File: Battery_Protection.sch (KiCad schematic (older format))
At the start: 0 parts

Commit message: Battery protection sch done. Assigned 99% of footprints. Layout is gonna be rough.
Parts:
- added C1, C10, C11, C2, C3, C4, C6, C7, C8, C9: C, Capacitor_SMD:C_0201_0603Metric, symbol Device:C
- added C12: 2.2u, Capacitor_SMD:C_0201_0603Metric, symbol Device:C
- added C13, C16: 0.1u 50v, Capacitor_SMD:C_0201_0603Metric, symbol Device:C
- added C14, C5: 0.1uF, Capacitor_SMD:C_0201_0603Metric, symbol Device:C
- added C15: 0.1u, Capacitor_SMD:C_0201_0603Metric, symbol Device:C
- added D1, D2, D3, D5, D6: LED, Diode_THT:D_DO-15_P3.81mm_Vertical_AnodeUp, symbol Device:LED
- added D4: DIODE, Diode_SMD:D_0201_0603Metric, symbol pspice:DIODE
- added F1, F2, F3, F4, F5, F6, F7, F8: Fuse_Small, Fuse:Fuse_1206_3216Metric_Pad1.42x1.75mm_HandSolder, symbol Device:Fuse_Small
- added J10, J11, J4, J5, J6, J7, J8, J9: Conn_01x02, Connector_JST:JST_PH_S2B-PH-K_1x02_P2.00mm_Horizontal, symbol Connector_Generic:Conn_01x02
- added Q1, Q6: 2n7002K, Package_TO_SOT_SMD:SOT-23, symbol Device:Q_NMOS_GSD
- added Q2, Q3, Q4, Q5: AO4468, Package_TO_SOT_SMD:TDSON-8-1, symbol Device:Q_NMOS_GSD
- added R1, R10, R2, R3, R4: 1k, Resistor_SMD:R_0201_0603Metric, symbol Device:R_US
- added R11, R12, R13, R19, R23, R24, R9: 100, Resistor_SMD:R_0201_0603Metric, symbol Device:R_US
- added R14: 51k, Resistor_SMD:R_0201_0603Metric, symbol Device:R_US
- added R15, R20, R22, R25, R29, R30: 5.1k, Resistor_SMD:R_0201_0603Metric, symbol Device:R_US
- added R16: 10Meg, Resistor_SMD:R_0201_0603Metric, symbol Device:R_US
- added R17: DNP, Resistor_SMD:R_0201_0603Metric, symbol Device:R_US
- added R18: 0, Resistor_SMD:R_0201_0603Metric, symbol Device:R_US
- added R21: 0.001, Resistor_SMD:R_1206_3216Metric, symbol Device:R_US
- added R26, R28: 10k, Resistor_SMD:R_0201_0603Metric, symbol Device:R_US
- added R27: 10M, Resistor_SMD:R_0201_0603Metric, symbol Device:R_US
- added R5, R6, R7, R8: 1 mOhm, Resistor_SMD:R_1206_3216Metric, symbol Device:R_US
- added SW1, SW2: SW_Push, Button_Switch_SMD:SW_Push_1P1T_NO_6x6mm_H9.5mm, symbol Switch:SW_Push
- added TH1: NCP18WF104F03, Resistor_SMD:R_0805_2012Metric, symbol Device:Thermistor_PTC
- added TH2, TH3, TH4, TH5: NXRT15WB473FA1B030, Diode_THT:D_A-405_P2.54mm_Vertical_AnodeUp, symbol Device:Thermistor_PTC_US
- added TP10, TP11, TP12, TP13, TP14, TP15, TP16, TP17, TP18, TP19, TP20, TP21, TP22, TP23, TP24, TP9: TestPoint, TestPoint:TestPoint_Pad_D2.0mm, symbol Connector:TestPoint
- added U101: BQ2947xx, Package_SON:WSON-8-1EP_2x2mm_P0.5mm_EP0.9x1.6mm, symbol SmartBattery:BQ2947xx
- added U102: BQ40Z50, Package_DFN_QFN:QFN-32-1EP_4x4mm_P0.4mm_EP2.65x2.65mm, symbol SmartBattery:BQ40Z50
- added U103: ITV4030, symbol SmartBattery:ITV4030
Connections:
- net labels added: BATT_SHUTDOWN, BAT_VN_0, BAT_VN_1, BAT_VN_2, BAT_VN_3, BAT_VP_0, BAT_VP_1, BAT_VP_2, BAT_VP_3, BTP_INT, FUSE_HEATER, GND, GNDA, PACK_+, SMB_C, SMB_D
- wire segments 0 -> 303
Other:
- note added: "LED = 333-2SURC/S530-A3\n5 mm DIP\n"

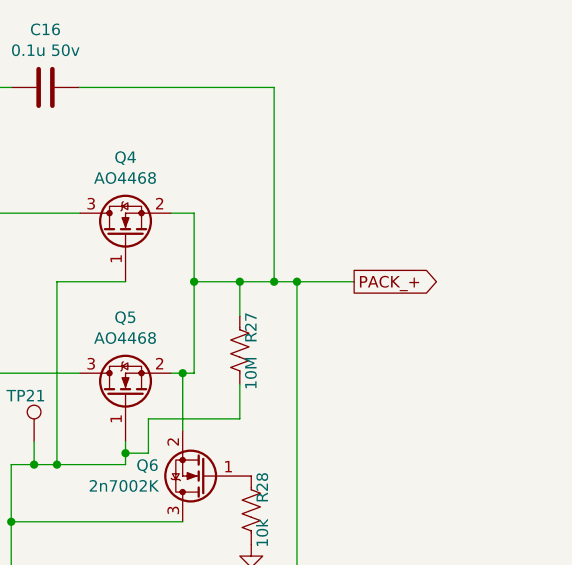
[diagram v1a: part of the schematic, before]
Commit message: Finished battery protection, starting charger page
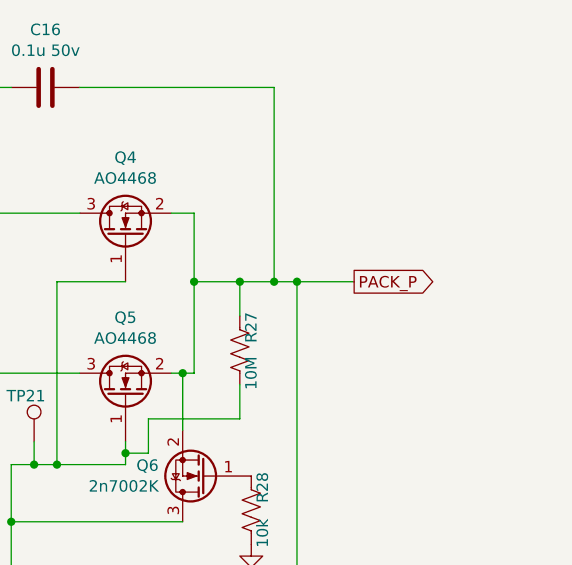
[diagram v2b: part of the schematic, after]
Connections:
- net labels added: PACK_P
- net labels removed: PACK_+
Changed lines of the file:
@@
 $Descr A4 11693 8268
 encoding utf-8
-Sheet 2 2
+Sheet 2 3
 Title ""
 Date ""
@@
 	8900 1650 8900 1350
 Text GLabel 9600 1650 2    50   Output ~ 0
-PACK_+
+PACK_P
 Connection ~ 9350 1650
 Wire Wire Line

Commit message: Added capacitors, inductors to charger page. Fixed capacitor sizes.
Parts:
- removed R7: 1 mOhm, Resistor_SMD:R_1206_3216Metric, symbol Device:R_US
- added TP18: TestPoint, TestPoint:TestPoint_Pad_D2.0mm, symbol Connector:TestPoint
- C18: renamed from C1; value C -> 0.1u 6.3v
- C19: renamed from C2; value C -> 0.1u 6.3v
- C20: renamed from C3; value C -> 0.1u 6.3v
- C21: renamed from C4; value C -> 0.1u 6.3v
- C22: renamed from C5; value 0.1uF -> 0.1uF 25v; footprint Capacitor_SMD:C_0201_0603Metric -> Capacitor_SMD:C_0402_1005Metric
- C23: renamed from C6; value C -> 0.1u 6.3v
- C24: renamed from C7; value C -> 0.1u 6.3v
- C25: renamed from C8; value C -> 0.1u 6.3v
- C26: renamed from C9; value C -> 0.1u 6.3v
- C27: renamed from C10; value C -> 0.1u 20v; footprint Capacitor_SMD:C_0201_0603Metric -> Capacitor_SMD:C_0402_1005Metric
- C28: renamed from C11; value C -> 0.1u 20v; footprint Capacitor_SMD:C_0201_0603Metric -> Capacitor_SMD:C_0402_1005Metric
- C29: renamed from C12; value 2.2u -> 2.2u 50v; footprint Capacitor_SMD:C_0201_0603Metric -> Capacitor_SMD:C_0603_1608Metric
- C30: renamed from C13; footprint Capacitor_SMD:C_0201_0603Metric -> Capacitor_SMD:C_0603_1608Metric
- C32: renamed from C15; value 0.1u -> 0.1u 6.3v
- C33: renamed from C16; footprint Capacitor_SMD:C_0201_0603Metric -> Capacitor_SMD:C_0603_1608Metric
- U2: renamed from U101; value BQ2947xx -> BQ294706DSGR
- renumbered C14 to C31, D1 to D2, D2 to D3, D3 to D4, D4 to D5, D5 to D6, D6 to D7, Q1 to Q2, Q2 to Q3, Q3 to Q4, Q4 to Q5, Q5 to Q6, Q6 to Q7, R8 to R10, R9 to R11, R10 to R12, R11 to R13, R12 to R14, R13 to R15, R14 to R16, R15 to R17, R16 to R18, R17 to R19, R18 to R20, R19 to R21, R20 to R22, R21 to R23, R22 to R24, R23 to R25, R24 to R26, R25 to R27, R26 to R28, R27 to R29, R1 to R3, R28 to R30, R29 to R31, R30 to R32, R2 to R4, R3 to R5, R4 to R6, R5 to R7, R6 to R8, TP17 to TP10, TP18 to TP11, TP19 to TP12, TP20 to TP13, TP21 to TP14, TP22 to TP15, TP23 to TP16, TP24 to TP17, TP9 to TP2, TP10 to TP3, TP11 to TP4, TP12 to TP5, TP13 to TP6, TP14 to TP7, TP15 to TP8, TP16 to TP9, U103 to U3, U102 to U4
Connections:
- net labels added: BATT_INT, BATT_PACK_P, BATT_SHUTDOWN_N, BATT_SMB_C, BATT_SMB_D
- net labels removed: BATT_SHUTDOWN, BTP_INT, PACK_P, SMB_C, SMB_D

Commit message: Added bunch of cap to charger, made footprint for diode + fuse
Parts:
- U3: footprint (none) -> SmartBattery:ITV4030
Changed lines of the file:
@@
 F 0 "U3" H 5600 2075 50  0000 C CNN
 F 1 "ITV4030" H 5600 1984 50  0000 C CNN
-F 2 "" H 5600 1700 50  0001 C CNN
+F 2 "SmartBattery:ITV4030" H 5600 1700 50  0001 C CNN
 F 3 "" H 5600 1700 50  0001 C CNN
 	1    5600 1700

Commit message: Adding lots of changes. Started output Stage
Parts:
- removed J10, J11, J4, J5, J6, J7, J8, J9: Conn_01x02, Connector_JST:JST_PH_S2B-PH-K_1x02_P2.00mm_Horizontal, symbol Connector_Generic:Conn_01x02
- removed Q3, Q4, Q5, Q6: AO4468, Package_TO_SOT_SMD:TDSON-8-1, symbol Device:Q_NMOS_GSD
- added J10, J11, J4, J5, J6, J7, J8, J9: JST 2P-1.0, Connector_JST:JST_SH_SM02B-SRSS-TB_1x02-1MP_P1.00mm_Horizontal, symbol Connector_Generic_MountingPin:Conn_01x02_MountingPin
- added Q4, Q6: AO4468, SmartBattery:SOIC-8_Alpha_Omega, symbol SmartBattery:AO4468

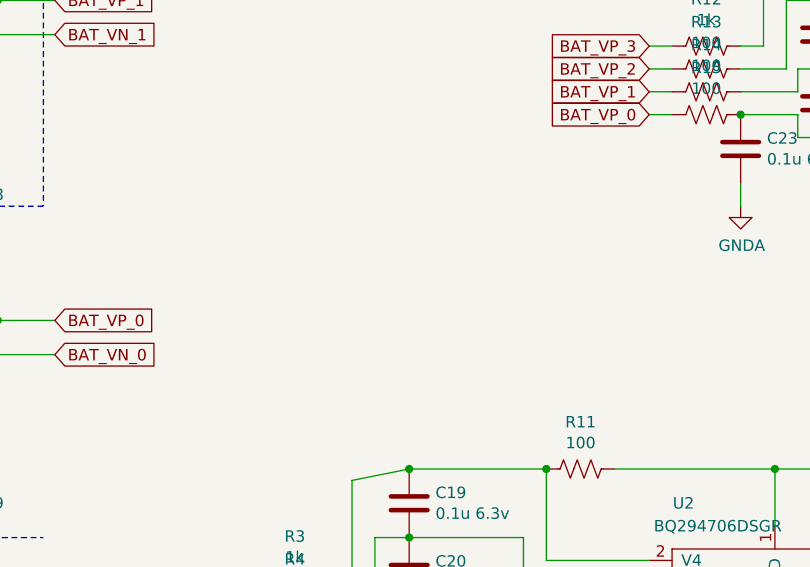
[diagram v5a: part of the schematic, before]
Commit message: Lots of changes for MFG: parts info
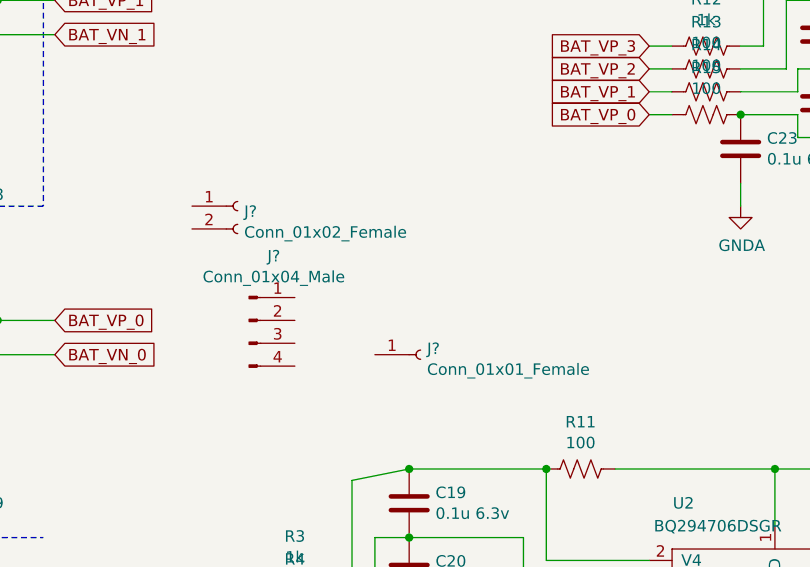
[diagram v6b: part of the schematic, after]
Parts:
- added J?: Conn_01x02_Female, symbol Connector:Conn_01x02_Female
- added J?: Conn_01x04_Male, symbol Connector:Conn_01x04_Male
- added J?: Conn_01x01_Female, symbol Connector:Conn_01x01_Female
- J10, J11, J4, J5, J6, J7, J8, J9: SKU (none) -> 320110054
- Q4, Q6: SKU (none) -> AO4468
- R11, R12, R13, R14, R15: SKU (none) -> 0201WMF1003TCE
- R22, R24, R26, R27, R31, R32: SKU (none) -> 0201WMJ0512TCE
- R3, R4, R5, R6: SKU (none) -> 0201WMF1001TCE
- SW1, SW2: SKU (none) -> B3F-1052
- TH1: SKU (none) -> NCP18WF104F03
- TH2, TH3, TH4, TH5: SKU (none) -> NXRT15WB473FA1B030
- U2: SKU (none) -> BQ294706DSGR
- U4: SKU (none) -> BQ40Z50RSMT-R2
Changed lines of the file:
@@
 F 2 "Package_SON:WSON-8-1EP_2x2mm_P0.5mm_EP0.9x1.6mm" H 4400 6900 50  0001 C CNN
 F 3 "" H 4400 6900 50  0001 C CNN
+F 4 "BQ294706DSGR" H 5100 6600 50  0001 C CNN "SKU"
 	1    5100 6600
 	1    0    0    -1
@@
 F 2 "Package_DFN_QFN:QFN-32-1EP_4x4mm_P0.4mm_EP2.65x2.65mm" H 7850 5000 50  0001 C CNN
 F 3 "" H 7850 5000 50  0001 C CNN
+F 4 "BQ40Z50RSMT-R2" H 7850 5000 50  0001 C CNN "SKU"
 	1    7850 5000
 	1    0    0    -1
@@
 F 2 "Resistor_SMD:R_0201_0603Metric" V 3140 6790 50  0001 C CNN
 F 3 "~" H 3100 6800 50  0001 C CNN
+F 4 "0201WMF1001TCE" V 3100 6800 50  0001 C CNN "SKU"
 	1    3100 6800
 	0    1    1    0
@@
 F 2 "Resistor_SMD:R_0201_0603Metric" V 3140 6690 50  0001 C CNN
 F 3 "~" H 3100 6700 50  0001 C CNN
+F 4 "0201WMF1001TCE" V 3100 6700 50  0001 C CNN "SKU"
 	1    3100 6700
 	0    1    1    0
@@
 F 2 "Resistor_SMD:R_0201_0603Metric" V 3140 6590 50  0001 C CNN
 F 3 "~" H 3100 6600 50  0001 C CNN
+F 4 "0201WMF1001TCE" V 3100 6600 50  0001 C CNN "SKU"
 	1    3100 6600
 	0    1    1    0
@@
 F 2 "Resistor_SMD:R_0201_0603Metric" V 3140 6490 50  0001 C CNN
 F 3 "~" H 3100 6500 50  0001 C CNN
+F 4 "0201WMF1001TCE" V 3100 6500 50  0001 C CNN "SKU"
 	1    3100 6500
 	0    1    1    0
@@
 F 2 "Resistor_SMD:R_0201_0603Metric" V 4390 5990 50  0001 C CNN
 F 3 "~" H 4350 6000 50  0001 C CNN
+F 4 "0201WMF1003TCE" V 4350 6000 50  0001 C CNN "SKU"
 	1    4350 6000
 	0    1    1    0
@@
 F 2 "Resistor_SMD:R_0201_0603Metric" V 4940 4440 50  0001 C CNN
 F 3 "~" H 4900 4450 50  0001 C CNN
+F 4 "0201WMF1003TCE" V 4900 4450 50  0001 C CNN "SKU"
 	1    4900 4450
 	0    1    1    0
@@
 F 2 "Resistor_SMD:R_0201_0603Metric" V 4940 4340 50  0001 C CNN
 F 3 "~" H 4900 4350 50  0001 C CNN
+F 4 "0201WMF1003TCE" V 4900 4350 50  0001 C CNN "SKU"
 	1    4900 4350
 	0    1    1    0
@@
 F 2 "Resistor_SMD:R_0201_0603Metric" V 4940 4240 50  0001 C CNN
 F 3 "~" H 4900 4250 50  0001 C CNN
+F 4 "0201WMF1003TCE" V 4900 4250 50  0001 C CNN "SKU"
 	1    4900 4250
 	0    1    1    0
@@
 F 2 "Resistor_SMD:R_0201_0603Metric" V 4940 4140 50  0001 C CNN
 F 3 "~" H 4900 4150 50  0001 C CNN
+F 4 "0201WMF1003TCE" V 4900 4150 50  0001 C CNN "SKU"
 	1    4900 4150
 	0    1    1    0
@@
 F 2 "Resistor_SMD:R_0805_2012Metric" H 7300 2900 50  0001 L CNN
 F 3 "~" H 7250 3100 50  0001 C CNN
+F 4 "NCP18WF104F03" V 7250 3100 50  0001 C CNN "SKU"
 	1    7250 3100
 	0    1    1    0
@@
 F 2 "Resistor_SMD:R_0201_0603Metric" V 7840 3340 50  0001 C CNN
 F 3 "~" H 7800 3350 50  0001 C CNN
+F 4 "0201WMJ0512TCE" V 7800 3350 50  0001 C CNN "SKU"
 	1    7800 3350
 	-1   0    0    1
@@
 F 2 "Resistor_SMD:R_0201_0603Metric" V 7940 3340 50  0001 C CNN
 F 3 "~" H 7900 3350 50  0001 C CNN
+F 4 "0201WMJ0512TCE" V 7900 3350 50  0001 C CNN "SKU"
 	1    7900 3350
 	-1   0    0    1
@@
 F 2 "Resistor_SMD:R_0201_0603Metric" V 8040 3340 50  0001 C CNN
 F 3 "~" H 8000 3350 50  0001 C CNN
+F 4 "0201WMJ0512TCE" V 8000 3350 50  0001 C CNN "SKU"
 	1    8000 3350
 	-1   0    0    1
@@
 F 2 "Resistor_SMD:R_0201_0603Metric" V 8140 3340 50  0001 C CNN
 F 3 "~" H 8100 3350 50  0001 C CNN
+F 4 "0201WMJ0512TCE" V 8100 3350 50  0001 C CNN "SKU"
 	1    8100 3350
 	-1   0    0    1
@@
 F 2 "Diode_THT:D_A-405_P2.54mm_Vertical_AnodeUp" H 9400 3900 50  0001 L CNN
 F 3 "~" H 9350 4100 50  0001 C CNN
+F 4 "NXRT15WB473FA1B030" V 9350 4100 50  0001 C CNN "SKU"
 	1    9350 4100
 	-1   0    0    1
@@
 F 2 "Diode_THT:D_A-405_P2.54mm_Vertical_AnodeUp" H 9600 3900 50  0001 L CNN
 F 3 "~" H 9550 4100 50  0001 C CNN
+F 4 "NXRT15WB473FA1B030" V 9550 4100 50  0001 C CNN "SKU"
 	1    9550 4100
 	-1   0    0    1
@@
 F 2 "Diode_THT:D_A-405_P2.54mm_Vertical_AnodeUp" H 9800 3900 50  0001 L CNN
 F 3 "~" H 9750 4100 50  0001 C CNN
+F 4 "NXRT15WB473FA1B030" V 9750 4100 50  0001 C CNN "SKU"
 	1    9750 4100
 	-1   0    0    1
@@
 F 2 "Diode_THT:D_A-405_P2.54mm_Vertical_AnodeUp" H 10000 3900 50  0001 L CNN
 F 3 "~" H 9950 4100 50  0001 C CNN
+F 4 "NXRT15WB473FA1B030" V 9950 4100 50  0001 C CNN "SKU"
 	1    9950 4100
 	-1   0    0    1
@@
 F 2 "Resistor_SMD:R_0201_0603Metric" V 9540 4540 50  0001 C CNN
 F 3 "~" H 9500 4550 50  0001 C CNN
+F 4 "0201WMJ0512TCE" V 9500 4550 50  0001 C CNN "SKU"
 	1    9500 4550
 	0    -1   -1   0
@@
 F 2 "Button_Switch_SMD:SW_Push_1P1T_NO_6x6mm_H9.5mm" H 10150 5250 50  0001 C CNN
 F 3 "~" H 10150 5250 50  0001 C CNN
+F 4 "B3F-1052" H 10150 5050 50  0001 C CNN "SKU"
 	1    10150 5050
 	1    0    0    -1
@@
 F 2 "Button_Switch_SMD:SW_Push_1P1T_NO_6x6mm_H9.5mm" H 10150 5600 50  0001 C CNN
 F 3 "~" H 10150 5600 50  0001 C CNN
+F 4 "B3F-1052" H 10150 5400 50  0001 C CNN "SKU"
 	1    10150 5400
 	1    0    0    -1
@@
 F 2 "Resistor_SMD:R_0201_0603Metric" V 9540 4690 50  0001 C CNN
 F 3 "~" H 9500 4700 50  0001 C CNN
+F 4 "0201WMJ0512TCE" V 9500 4700 50  0001 C CNN "SKU"
 	1    9500 4700
 	0    -1   -1   0
@@
 F 2 "Connector_JST:JST_SH_SM02B-SRSS-TB_1x02-1MP_P1.00mm_Horizontal" H 950 5800 50  0001 C CNN
 F 3 "~" H 950 5800 50  0001 C CNN
+F 4 "320110054" H 950 5800 50  0001 C CNN "SKU"
 	1    950  5800
 	-1   0    0    -1
@@
 F 2 "Connector_JST:JST_SH_SM02B-SRSS-TB_1x02-1MP_P1.00mm_Horizontal" H 950 5150 50  0001 C CNN
 F 3 "~" H 950 5150 50  0001 C CNN
+F 4 "320110054" H 950 5150 50  0001 C CNN "SKU"
 	1    950  5150
 	-1   0    0    -1
@@
 F 2 "Connector_JST:JST_SH_SM02B-SRSS-TB_1x02-1MP_P1.00mm_Horizontal" H 950 3800 50  0001 C CNN
 F 3 "~" H 950 3800 50  0001 C CNN
+F 4 "320110054" H 950 3800 50  0001 C CNN "SKU"
 	1    950  3800
 	-1   0    0    -1
@@
 F 2 "Connector_JST:JST_SH_SM02B-SRSS-TB_1x02-1MP_P1.00mm_Horizontal" H 950 4450 50  0001 C CNN
 F 3 "~" H 950 4450 50  0001 C CNN
+F 4 "320110054" H 950 4450 50  0001 C CNN "SKU"
 	1    950  4450
 	-1   0    0    -1
@@
 F 2 "Connector_JST:JST_SH_SM02B-SRSS-TB_1x02-1MP_P1.00mm_Horizontal" H 950 2450 50  0001 C CNN
 F 3 "~" H 950 2450 50  0001 C CNN
+F 4 "320110054" H 950 2450 50  0001 C CNN "SKU"
 	1    950  2450
 	-1   0    0    -1
@@
 F 2 "Connector_JST:JST_SH_SM02B-SRSS-TB_1x02-1MP_P1.00mm_Horizontal" H 950 3100 50  0001 C CNN
 F 3 "~" H 950 3100 50  0001 C CNN
+F 4 "320110054" H 950 3100 50  0001 C CNN "SKU"
 	1    950  3100
 	-1   0    0    -1
@@
 F 2 "Connector_JST:JST_SH_SM02B-SRSS-TB_1x02-1MP_P1.00mm_Horizontal" H 950 1100 50  0001 C CNN
 F 3 "~" H 950 1100 50  0001 C CNN
+F 4 "320110054" H 950 1100 50  0001 C CNN "SKU"
 	1    950  1100
 	-1   0    0    -1
@@
 F 2 "Connector_JST:JST_SH_SM02B-SRSS-TB_1x02-1MP_P1.00mm_Horizontal" H 950 1750 50  0001 C CNN
 F 3 "~" H 950 1750 50  0001 C CNN
+F 4 "320110054" H 950 1750 50  0001 C CNN "SKU"
 	1    950  1750
 	-1   0    0    -1
@@
 F 2 "SmartBattery:SOIC-8_Alpha_Omega" H 7000 2050 50  0001 C CNN
 F 3 "~" H 6800 1950 50  0001 C CNN
+F 4 "AO4468" V 6800 1950 50  0001 C CNN "SKU"
 	1    6800 1950
 	0    1    1    0
@@
 F 2 "SmartBattery:SOIC-8_Alpha_Omega" H 8800 2250 50  0001 C CNN
 F 3 "~" H 8600 2150 50  0001 C CNN
+F 4 "AO4468" V 8600 2150 50  0001 C CNN "SKU"
 	1    8600 2150
 	0    -1   -1   0
 $EndComp
+$Comp
+L Connector:Conn_01x02_Female J?
+U 1 1 5FE89E75
+P 2850 4850
+F 0 "J?" H 2878 4826 50  0000 L CNN
+F 1 "Conn_01x02_Female" H 2878 4735 50  0000 L CNN
+F 2 "" H 2850 4850 50  0001 C CNN
+F 3 "~" H 2850 4850 50  0001 C CNN
+	1    2850 4850
+	1    0    0    -1
+$EndComp
+$Comp
+L Connector:Conn_01x04_Male J?
+U 1 1 5FE8B251
+P 2900 5350
+F 0 "J?" H 3008 5631 50  0000 C CNN
+F 1 "Conn_01x04_Male" H 3008 5540 50  0000 C CNN
+F 2 "" H 2900 5350 50  0001 C CNN
+F 3 "~" H 2900 5350 50  0001 C CNN
+	1    2900 5350
+	1    0    0    -1
+$EndComp
+$Comp
+L Connector:Conn_01x01_Female J?
+U 1 1 5FE8E98D
+P 3650 5500
+F 0 "J?" H 3678 5526 50  0000 L CNN
+F 1 "Conn_01x01_Female" H 3678 5435 50  0000 L CNN
+F 2 "" H 3650 5500 50  0001 C CNN
+F 3 "~" H 3650 5500 50  0001 C CNN
+	1    3650 5500
+	1    0    0    -1
+$EndComp
 $EndSCHEMATC
